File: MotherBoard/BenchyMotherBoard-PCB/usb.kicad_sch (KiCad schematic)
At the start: 1 part

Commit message: Add MORE regulators, USB, Display, and SDCard
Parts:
- added J? (x6): USB3_A, symbol Connector:USB3_A
- added U? (x3): USB7206C, SnapEDA:QFN40P1200X1200X90-101N, symbol Daxxn_IC:USB7206C
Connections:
- net MPU-USB-D+: now reaches U?.V14 (USB-DP1)
- net MPU-USB-D+: now also U?.42 (USBD-DP6)
- net MPU-USB-D-: now reaches U?.W14 (USB-DM1)
- net MPU-USB-D-: now also U?.41 (USBD-DM6)
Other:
- company: (none) -> Daxxn Industries
- title: (none) -> Benchy Version 2
- moved on the sheet: U?D

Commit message: Initial schematic lock
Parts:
- removed J?: USB3_A, symbol Connector:USB3_A
- removed U? (x2): USB7206C, SnapEDA:QFN40P1200X1200X90-101N, symbol Daxxn_IC:USB7206C
- added C139, C140, C142, C143, C144, C145, C146, C147, C148, C149, C156, C160, C? (x2): 10uF, Capacitor_SMD:C_1210_3225Metric, symbol Device:C_Small
- added C141, C150, C151, C152, C153, C154, C155, C163, C164: 100nF, Capacitor_SMD:C_0402_1005Metric, symbol Device:C_Small
- added C157, C161: 1uF, Capacitor_SMD:C_1210_3225Metric, symbol Device:C_Small
- added C158, C159, C162, C165: 15pF, Capacitor_SMD:C_0402_1005Metric, symbol Device:C_Small
- added C? (x3): 1uF, Capacitor_SMD:C_0805_2012Metric, symbol Device:C_Small
- added C?: 100nF, Capacitor_SMD:C_0805_2012Metric, symbol Device:C_Small
- added D1, D2, D3, D4, D5: ESDLC5V0PB8, Package_DFN_QFN:UDFN-9_1.0x3.8mm_P0.5mm, symbol Power_Protection:ESDLC5V0PB8
- added D6: PUSB3AB4, Daxxn_Packages:DFN2510A-10, symbol Daxxn_Protection:PUSB3AB4
- added D7: ORANGE, Daxxn_LEDs:LED-SMD-1204_RA, symbol Device:LED_Small
- added D8: YELLOW, Daxxn_LEDs:LED-SMD-1204_RA, symbol Device:LED_Small
- added J13, J14: USB_A, Daxxn_Connectors:1002-014-01000, symbol Connector:USB_A
- added J8: USB3_B, Daxxn_Connectors:USB-GSB3211311WEU, symbol Connector:USB3_B
- added J?: TFT-DISPLAY, symbol Connector:Conn_01x21_Male
- added JP1: WP-JMP, Connector_PinSocket_2.54mm:PinSocket_1x03_P2.54mm_Vertical, symbol Jumper:Jumper_3_Bridged12
- added Q?: RQ5A030AP, Package_TO_SOT_SMD:SOT-23, symbol Daxxn_Transistors:RQ5A030AP
- added R100: 3K, Resistor_SMD:R_0402_1005Metric, symbol Device:R_Small_US
- added R101, R107, R92, R93, R94, R95: 10K, Resistor_SMD:R_0402_1005Metric, symbol Device:R_Small_US
- added R102: 12K 1%, Resistor_SMD:R_0402_1005Metric, symbol Device:R_Small_US
- added R103, R104, R88: 50K, Resistor_SMD:R_0402_1005Metric, symbol Device:R_Small_US
- added R105, R106: 1K, Resistor_SMD:R_0402_1005Metric, symbol Device:R_Small_US
- added R108, R96, R97: 200K, Resistor_SMD:R_0402_1005Metric, symbol Device:R_Small_US
- added R87: 43K, Resistor_SMD:R_0402_1005Metric, symbol Device:R_Small_US
- added R89, R90, R91: 18K, Resistor_SMD:R_0402_1005Metric, symbol Device:R_Small_US
- added R98, R99, R? (x2): 2.2K, Resistor_SMD:R_0402_1005Metric, symbol Device:R_Small_US
- added R?: 10 1%, Resistor_SMD:R_0805_2012Metric, symbol Device:R_Small_US
- added R?: 330, Resistor_SMD:R_0805_2012Metric, symbol Device:R_Small_US
- added R?: 120, Resistor_SMD:R_0805_2012Metric, symbol Device:R_Small_US
- added R?: 10K, Daxxn_Switches:Bourns_TC33X, symbol Daxxn_Other:R_Pot_Small_US
- added U12, U13, U14: UCS2114, Daxxn_Packages:UCS2114T-1-V_LXVAO-Custom, symbol Daxxn_IC:UCS2114
- added U15: 24LC08, Package_SO:SOIC-8_3.9x4.9mm_P1.27mm, symbol Memory_EEPROM:24LC08
- added U16: USB2412, Package_DFN_QFN:QFN-28-1EP_5x5mm_P0.5mm_EP3.35x3.35mm, symbol Daxxn_IC:USB2412
- added unit 2 of U9
- added unit 3 of U9
- added U?: AS321, Package_TO_SOT_SMD:SOT-23-5, symbol Daxxn_OPAMP:AS321
- added U?: LM317L, Package_TO_SOT_SMD:SOT-89-3, symbol Regulator_Linear:LM317L_SOT-89
- added Y3, Y4: 25MHz, Daxxn_Passives:Crystal_SMD_4Pin_3.2x2.5mm, symbol Device:Crystal_GND24_Small
- J10, J11, J12, J7, J9: renamed from J?; footprint (none) -> Connector_USB:USB3_A_Molex_48393-001
- gave numbers to parts that had none: 2
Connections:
- net DSI-D0-: now reaches U2.A13 (DSI-D0N)
- net DSI-D0-: now also J?.18 (Pin_18)
- net DSI-CL-: now reaches U2.A14 (DSI-CKN)
- net DSI-CL-: now also J?.15 (Pin_15)
- net DSI-D1-: now reaches U2.A15 (DSI-D1N)
- net DSI-D1-: now also J?.12 (Pin_12)
- net DSI-D0+: now reaches U2.B13 (DSI-D0P)
- net DSI-D0+: now also J?.17 (Pin_17)
- net DSI-CL+: now reaches U2.B14 (DSI-CKP)
- net DSI-CL+: now also J?.14 (Pin_14)
- net DSI-D1+: now reaches U2.B15 (DSI-D1P)
- net DSI-D1+: now also J?.11 (Pin_11)
- net USB-INU-D-: now reaches U2.V13 (USB-DM2)
- net USB-INU-D-: now also U16.21 (USBU-)
- net at U2.V16 (USB-RREF): now also R100.1
- net USB-INU-D+: now reaches U2.W13 (USB-DP2)
- net USB-INU-D+: now also U16.22 (USBU+)
- net at J11.1 (VBUS): now also C147.2, U13.11 (VBUS2), U13.12 (VBUS2)
- net GND: now reaches J11.10 (SHIELD)
- net GND: now also J10.10 (SHIELD), J10.4 (GND), J10.7 (DRAIN), J11.4 (GND), J11.7 (DRAIN), J12.10 (SHIELD), J12.4 (GND), J12.7 (DRAIN), J7.10 (SHIELD), J7.4 (GND), J7.7 (DRAIN), J9.10 (SHIELD), J9.4 (GND), J9.7 (DRAIN), C139.1, C140.1, C141.1, C142.1, C143.1, C144.1, C145.1, C146.1, C147.1, C148.1, C149.1, C150.1, C151.1, C152.1, C153.1, C154.1, C155.1, C156.1, C157.1, C158.2, C159.1, C160.1, C161.1, C162.2, C163.1, C164.1, C165.1, C?.2, C?.2, C?.2, C?.2, C?.2, C?.2, D1.3 (A), D2.3 (A), D3.3 (A), D4.3 (A), D5.3 (A), D6.3 (A), D6.8 (A), J13.4 (GND), J13.5 (Shield), J14.4 (GND), J14.5 (Shield), J8.10 (SHIELD), J8.4 (GND), J8.7 (DRAIN), J?.10 (Pin_10), J?.13 (Pin_13), J?.16 (Pin_16), J?.19 (Pin_19), J?.2 (Pin_2), J?.20 (Pin_20), J?.21 (Pin_21), JP1.3 (B), R100.2, R102.2, R103.2, R104.2, R105.2, R106.2, R107.1, R108.1, R88.2, R89.2, R90.2, R91.2, R95.1, R96.1, R97.1, R?.3, U12.13 (BOOST), U12.14 (GND), U12.17 (GND), U12.2 (GND), U13.13 (BOOST), U13.14 (GND), U13.17 (GND), U13.2 (GND), U14.13 (BOOST), U14.14 (GND), U14.15 (EN2), U14.16 (ALERT2), U14.17 (GND), U14.2 (GND), U15.1 (A0), U15.2 (A1), U15.3 (A2), U15.4 (GND), U16.15 (TEST1), U16.29 (GND), U16.6 (TEST), U9.24 (TESTEN), U?.2 (V-), Y3.2, Y3.4, Y4.2, Y4.4
- net USB4-D-: now reaches J11.2 (D-)
- net USB4-D-: now also U9.35 (USBD-DM4), D4.2 (K2)
- net USB4-D+: now reaches J11.3 (D+)
- net USB4-D+: now also U9.34 (USBD-DP4), D4.4 (K3)
- net USB4-TX-: now reaches J11.5 (SSRX-)
- net USB4-TX-: now also U9.37 (USBD-TXM4), D4.5 (K4)
- net USB4-TX+: now reaches J11.6 (SSRX+)
- net USB4-TX+: now also U9.36 (USBD-TXP4), D4.6 (K5)
- net USB4-RX-: now reaches J11.8 (SSTX-)
- net USB4-RX-: now also U9.40 (USBD-RXM4), D4.7 (K6)
- net USB4-RX+: now reaches J11.9 (SSTX+)
- net USB4-RX+: now also U9.39 (USBD-RXP4), D4.8 (K7)
- net at J7.1 (VBUS): now also C140.2, U12.4 (VBUS1), U12.5 (VBUS1)
- net USB1-D-: now reaches J7.2 (D-)
- net USB1-D-: now also U9.6 (USBD-DM1), D1.2 (K2)
- net USB1-D+: now reaches J7.3 (D+)
- net USB1-D+: now also U9.5 (USBD-DP1), D1.4 (K3)
- net USB1-TX-: now reaches J7.5 (SSRX-)
- net USB1-TX-: now also U9.8 (USBD-TXM1), D1.5 (K4)
- net USB1-TX+: now reaches J7.6 (SSRX+)
- net USB1-TX+: now also U9.7 (USBD-TXP1), D1.6 (K5)
- net USB1-RX-: now reaches J7.8 (SSTX-)
- net USB1-RX-: now also U9.11 (USBD-RXM1), D1.7 (K6)
- net USB1-RX+: now reaches J7.9 (SSTX+)
- net USB1-RX+: now also U9.10 (USBD-RXP1), D1.8 (K7)
- net USB2-D+: now reaches U9.14 (USBD-DP2)
- net USB2-D+: now also J9.3 (D+), D2.4 (K3)
- net USB2-D-: now reaches U9.15 (USBD-DM2)
- net USB2-D-: now also J9.2 (D-), D2.2 (K2)
- net USB2-TX+: now reaches U9.16 (USBD-TXP2)
- net USB2-TX+: now also J9.6 (SSRX+), D2.6 (K5)
- net USB2-TX-: now reaches U9.17 (USBD-TXM2)
- net USB2-TX-: now also J9.5 (SSRX-), D2.5 (K4)
- net USB2-RX+: now reaches U9.19 (USBD-RXP2)
- net USB2-RX+: now also J9.9 (SSTX+), D2.8 (K7)
- net at U9.2 (VBUS-MON): now also R87.2, R88.1
- net USB2-RX-: now reaches U9.20 (USBD-RXM2)
- net USB2-RX-: now also J9.8 (SSTX-), D2.7 (K6)
- net USB3-D+: now reaches U9.27 (USBD-DP3)
- net USB3-D+: now also J10.3 (D+), D3.4 (K3)
- net USB3-D-: now reaches U9.28 (USBD-DM3)
- net USB3-D-: now also J10.2 (D-), D3.2 (K2)
- net USB3-TX+: now reaches U9.29 (USBD-TXP3)
- net USB3-TX+: now also J10.6 (SSRX+), D3.6 (K5)
- net USB3-TX-: now reaches U9.30 (USBD-TXM3)
- net USB3-TX-: now also J10.5 (SSRX-), D3.5 (K4)
- net USB3-RX+: now reaches U9.32 (USBD-RXP3)
- net USB3-RX+: now also J10.9 (SSTX+), D3.8 (K7)
- net USB3-RX-: now reaches U9.33 (USBD-RXM3)
- net USB3-RX-: now also J10.8 (SSTX-), D3.7 (K6)
- net USB5-D+: now reaches U9.81 (USBD-DP5)
- net USB5-D+: now also J12.3 (D+), D5.4 (K3)
- net USB5-D-: now reaches U9.82 (USBD-DM5)
- net USB5-D-: now also J12.2 (D-), D5.2 (K2)
- net USB5-TX+: now reaches U9.83 (USBD-TXP5)
- net USB5-TX+: now also J12.6 (SSRX+), D5.6 (K5)
- net USB5-TX-: now reaches U9.84 (USBD-TXM5)
- net USB5-TX-: now also J12.5 (SSRX-), D5.5 (K4)
- net USB5-RX+: now reaches U9.86 (USBD-RXP5)
- net USB5-RX+: now also J12.9 (SSTX+), D5.8 (K7)
- net USB5-RX-: now reaches U9.87 (USBD-RXM5)
- net USB5-RX-: now also J12.8 (SSTX-), D5.7 (K6)
- net USBU-D+: now reaches U9.89 (USBU-DP)
- net USBU-D+: now also J8.3 (D+)
- net USBU-D-: now reaches U9.90 (USBU-DM)
- net USBU-D-: now also J8.2 (D-)
- net USBU-TX+: now reaches U9.91 (USBU-TXP)
- net USBU-TX+: now also J8.6 (SSTX+)
- net USBU-TX-: now reaches U9.92 (USBU-TXM)
- net USBU-TX-: now also J8.5 (SSTX-)
- net USBU-RX+: now reaches U9.94 (USBU-RXP)
- net USBU-RX+: now also J8.9 (SSRX+)
- net USBU-RX-: now reaches U9.95 (USBU-RXM)
- net USBU-RX-: now also J8.8 (SSRX-)
- net at J9.1 (VBUS): now also C143.2, U12.11 (VBUS2), U12.12 (VBUS2)
- net at J12.1 (VBUS): now also C149.2, U14.4 (VBUS1), U14.5 (VBUS1)
- net at J10.1 (VBUS): now also C145.2, U13.4 (VBUS1), U13.5 (VBUS1)
- net MPU-USB-D+ renamed USB-MPU-D+
- net MPU-USB-D- renamed USB-MPU-D-
- new net: R104.1, U16.13 (NON-REM1)
- new net: C162.1, U9.97 (XTAL0), Y4.1
- new net: Q?.1 (G), R?.2
- new net: Q?.3 (D), R?.2, U?.3 (IN-)
- new net: R98.1, U15.6 (SCL), U9.3 (PF31)
- new net: R96.2, U9.22 (CFG-STRAP2)
- new net: R92.1, U9.63 (TEST1)
- new net: D7.2 (A), R103.1, U16.19 (SUSP-IND/NON-REM0)
- new net: C?.1, C?.1, R?.1, R?.1, U?.2 (VO)
- new net: D7.1 (K), R105.1
- new net: C141.2, J8.1 (VBUS), R87.1
- new net: C?.1, R?.2, U?.1 (IN+)
- new net: R?.1, U?.4 (OUT)
- new net: R97.2, U9.23 (CFG-STRAP3)
- new net: JP1.2 (C), U15.7 (WP)
- new net: R?.2, U?.1 (ADJ)
- new net: R95.2, U9.21 (CFG-STRAP1)
- new net: R99.1, U15.5 (SDA), U9.61 (PF18)
- new net: R93.1, U9.64 (TEST2)
- new net: R94.1, U9.65 (TEST3)
- new net: C163.2, U16.9 (CRFILT)
- new net: D8.2 (A), U16.16 (HS-IND)
- new net: C158.1, U16.23 (XTALOUT), Y3.1
- new net: C159.2, U16.24 (XTALIN), Y3.3
- new net: C164.2, U16.25 (PLLFILT)
- new net: R102.1, U16.26 (RBIAS)
- new net: C165.2, U9.98 (XTAL1), Y4.3
- new net: R91.1, U14.3 (COMM-EN)
- new net: D8.1 (K), R106.1
- new net: D6.10 (NC), D6.6 (NC), D6.7 (NC), D6.9 (NC)
- new net: R89.1, U12.3 (COMM-EN)
- new net: R108.2, U9.70 (SPI-D0)
- new net: R90.1, U13.3 (COMM-EN)
- new net: R107.2, U9.69 (~{SPI_CE})
- new net +30V: C?.1, C?.1, C?.1, U?.3 (VI), U?.5 (V+)
- new net BK-ANODE: J?.4 (Pin_4), Q?.2 (S)
- new net DISP-USB-BUS.BRIGHT: R?.1
- new net DISP-USB-BUS.TE: J?.8 (Pin_8)
- new net DISP-USB-BUS.USB-RESET: R101.1, U16.17 (~{RESET}), U9.1 (~{RESET})
- new net DISP-USB-BUS.USB-SCK: R?.2, U12.19 (I2C-SCLK), U13.19 (I2C-SCLK), U14.19 (I2C-SCLK)
- new net DISP-USB-BUS.USB-SDA: R?.2, U12.18 (I2C-SDA), U13.18 (I2C-SDA), U14.18 (I2C-SDA)
- new net RESET: J?.9 (Pin_9)
- new net USB-IN1-D+: D6.1 (K1), J13.3 (D+), U16.1 (USBD1-D+)
- new net USB-IN1-D-: D6.2 (K2), J13.2 (D-), U16.28 (USBD1-)
- new net USB-IN2-D+: D6.4 (K3), J14.3 (D+), U16.3 (USBD2-D+)
- new net USB-IN2-D-: D6.5 (K4), J14.2 (D-), U16.2 (USBD2-D-)
- new net USB1-EN-~{OC}: U12.1 (EN1), U12.20 (ALERT1), U9.60 (PF17)
- new net USB2-EN-~{OC}: U12.15 (EN2), U12.16 (ALERT2), U9.59 (PF16)
- new net USB3-EN-~{OC}: U13.1 (EN1), U13.20 (ALERT1), U9.58 (PF15)
- new net USB4-EN-~{OC}: U13.15 (EN2), U13.16 (ALERT2), U9.57 (PF14)
- new net USB5-EN-~{OC}: U14.1 (EN1), U14.20 (ALERT1), U9.56 (PF13)
- new net VCC: C139.2, C142.2, C144.2, C146.2, C148.2, C156.2, C157.2, C160.2, C161.2, J13.1 (VBUS), J14.1 (VBUS), U12.10 (VS), U12.6 (VS), U12.7 (VS), U12.8 (VDD), U12.9 (VS), U13.10 (VS), U13.6 (VS), U13.7 (VS), U13.8 (VDD), U13.9 (VS), U14.6 (VS), U14.7 (VS), U14.8 (VDD)
- new net VDD: C150.2, C151.2, C152.2, C153.2, C154.2, C155.2, J?.6 (Pin_6), J?.7 (Pin_7), JP1.1 (A), R101.2, R92.2, R93.2, R94.2, R98.2, R99.2, R?.1, R?.1, U15.8 (VCC), U16.10 (VDD), U16.14 (VDD), U16.20 (VDD), U16.27 (VDD), U16.4 (VDD)
- no-connect marks 0 -> 38
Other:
- moved on the sheet: J10, J11, J12, J7, J9, U2D

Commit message: (WIP) Start layout
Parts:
- J11: renamed from J9; footprint Connector_USB:USB3_A_Molex_48393-001 -> Daxxn_Connectors:GSB4116341HR
- J12: renamed from J10; footprint Connector_USB:USB3_A_Molex_48393-001 -> Daxxn_Connectors:GSB4116341HR
- J13: renamed from J11; footprint Connector_USB:USB3_A_Molex_48393-001 -> Daxxn_Connectors:GSB4116341HR
- J14: renamed from J12; footprint Connector_USB:USB3_A_Molex_48393-001 -> Daxxn_Connectors:GSB4116341HR
- J16: renamed from J?; footprint (none) -> Daxxn_Connectors:FH12A-20S-0.5SH55
- J9: renamed from J7; footprint Connector_USB:USB3_A_Molex_48393-001 -> Daxxn_Connectors:GSB4116341HR
- U10: renamed from U9; footprint SnapEDA:QFN40P1200X1200X90-101N -> Daxxn_Packages:100-VQFN-GND_12X12
- gave numbers to parts that had none: 15
- renumbered C139 to C141, C140 to C142, C141 to C143, C142 to C144, C143 to C145, C144 to C146, C145 to C147, C146 to C148, C147 to C149, C148 to C150, C149 to C151, C150 to C158, C151 to C159, C152 to C160, C153 to C161, C154 to C162, C155 to C163, C156 to C164, C157 to C165, C158 to C166, C159 to C167, C160 to C168, C161 to C169, C162 to C170, C163 to C171, C164 to C172, C165 to C173, J8 to J10, J13 to J15, J14 to J17, JP1 to JP2, R91 to R100, R92 to R101, R93 to R102, R94 to R103, R95 to R108, R96 to R109, R97 to R110, R98 to R111, R99 to R112, R100 to R113, R101 to R114, R102 to R115, R103 to R116, R104 to R117, R105 to R118, R106 to R119, R107 to R120, R108 to R121, R87 to R94, R88 to R95, R89 to R98, R90 to R99, U9 to U10, U12 to U13, U13 to U14, U14 to U15, U15 to U18, U16 to U19
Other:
- title: Benchy Version 2 -> Benchy Reloaded

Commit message: (WIP) Replaced DDR VRef with reg and started layout
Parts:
- added D9: ESDLC5V0PB8, Package_DFN_QFN:UDFN-9_1.0x3.8mm_P0.5mm, symbol Power_Protection:ESDLC5V0PB8
- J11: value USB3_A -> USB3-PORT2
- J12: value USB3_A -> USB3-PORT3
- J13: value USB3_A -> USB3-PORT4
- J14: value USB3_A -> USB3-PORT5
- J15: value USB_A -> USB-INTERNAL-PORT1
- J17: value USB_A -> USB-INTERNAL-PORT2
- J9: value USB3_A -> USB3-PORT1
- U10: footprint SnapEDA:QFN40P1200X1200X90-101N -> Daxxn_Packages:100-VQFN-GND_12X12
- renumbered C141 to C145, C142 to C146, C143 to C147, C144 to C148, C145 to C149, C146 to C150, C147 to C151, C148 to C152, C149 to C153, C150 to C154, C151 to C155, C152 to C156, C153 to C157, C154 to C158, C155 to C159, C156 to C160, C157 to C161, C158 to C162, C159 to C163, C160 to C164, C161 to C165, C162 to C166, C163 to C167, C164 to C168, C165 to C169, C166 to C170, C167 to C171, C168 to C172, C169 to C173, C170 to C174, C171 to C175, C172 to C176, C173 to C177, R103 to R100, R104 to R101, R105 to R102, R106 to R103, R107 to R104, R108 to R105, R109 to R106, R110 to R107, R111 to R108, R112 to R109, R113 to R110, R114 to R111, R115 to R112, R116 to R113, R117 to R114, R118 to R115, R119 to R116, R120 to R117, R121 to R118, R94 to R91, R95 to R92, R96 to R93, R97 to R94, R98 to R95, R99 to R96, R100 to R97, R101 to R98, R102 to R99, U2 to U1, U13 to U12, U14 to U13, U15 to U14, U16 to U15, U17 to U16, U18 to U17, U19 to U18
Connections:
- net DSI-CL+: now also D9.8 (K7)
- net DSI-CL-: now also D9.7 (K6)
- net DSI-D0+: now also D9.4 (K3)
- net DSI-D0-: now also D9.6 (K5)
- net DSI-D1+: now also D9.9 (K8)
- net DSI-D1-: now also D9.2 (K2)
- net GND: now also D9.3 (A)
- net USB-NONREM1: now reaches R114.1, U18.13 (NON-REM1)
- net USBP2-VBUS: now reaches C149.2, J11.1 (VBUS), U12.11 (VBUS2), U12.12 (VBUS2)
- net USB-SUSP-IND: now reaches D7.2 (A), R113.1, U18.19 (SUSP-IND/NON-REM0)
- net USB-RREF: now reaches R110.1, U1.V16 (USB-RREF)
- net USBP1-VBUS: now reaches C146.2, J9.1 (VBUS), U12.4 (VBUS1), U12.5 (VBUS1)
- net USBP4-VBUS: now reaches C153.2, J13.1 (VBUS), U13.11 (VBUS2), U13.12 (VBUS2)
- net USB-HS-IND: now reaches D8.2 (A), U18.16 (HS-IND)
- net USB-IN-XIN: now reaches C170.1, Y3.1
- net USB-IN-XIN: now also U18.24 (XTALIN); no longer U18.23 (XTALOUT)
- net USB-IN-XOUT: now reaches C171.2, Y3.3
- net USB-IN-XOUT: now also U18.23 (XTALOUT); no longer U18.24 (XTALIN)
- net USBP3-VBUS: now reaches C151.2, J12.1 (VBUS), U13.4 (VBUS1), U13.5 (VBUS1)
- net USB13-COMM: now reaches R97.1, U14.3 (COMM-EN)
- net USB13-COMM: now also R96.1, U13.3 (COMM-EN)
- net USB12-COMM: now reaches R95.1, U12.3 (COMM-EN)
- net USBP5-VBUS: now reaches C155.2, J14.1 (VBUS), U14.4 (VBUS1), U14.5 (VBUS1)
- net DISP-USB-BUS.BRIGHT renamed USB-BUS.BRIGHT
- net DISP-USB-BUS.TE renamed DISP-BUS.TE
- net DISP-USB-BUS.USB-RESET renamed USB-BUS.RESET
- net DISP-USB-BUS.USB-SCK renamed USB-BUS.SCK
- net DISP-USB-BUS.USB-SDA renamed USB-BUS.SDA
- net RESET renamed DISP-BUS.RESET
- no-connect marks 38 -> 40
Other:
- moved on the sheet: C145, C146, C147, C148, C149, C150, C151, C152, C153, C154, C155, C156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

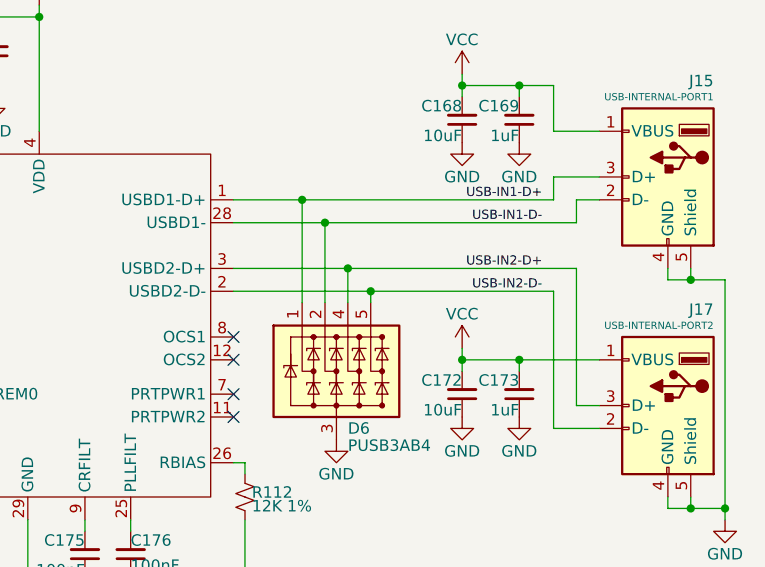
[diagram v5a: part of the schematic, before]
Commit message: Finish DDR3 memory layout
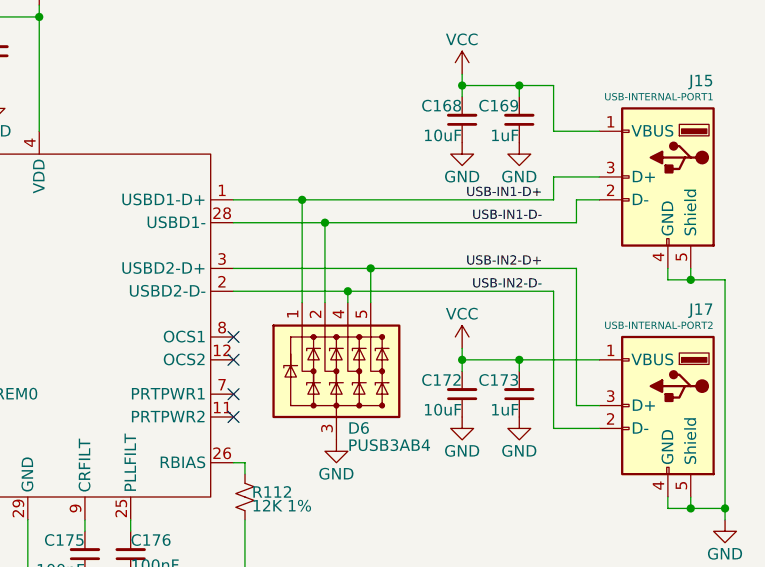
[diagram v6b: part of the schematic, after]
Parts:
- D1, D2, D3, D4, D5, D9: footprint Package_DFN_QFN:UDFN-9_1.0x3.8mm_P0.5mm -> Daxxn_Packages:U-DFN3810-9
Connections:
- net USB-IN2-D+: now also D6.5 (K4); no longer D6.4 (K3)
- net USB-IN2-D-: now also D6.4 (K3); no longer D6.5 (K4)
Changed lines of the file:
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@@
   (junction (at 204.47 24.13) (diameter 0) (color 0 0 0 0)
   )
-  (junction (at 365.76 212.09) (diameter 0) (color 0 0 0 0)
-  )
   (junction (at 168.91 226.06) (diameter 0) (color 0 0 0 0)
   )
@@
   (junction (at 401.32 78.74) (diameter 0) (color 0 0 0 0)
   )
+  (junction (at 363.22 212.09) (diameter 0) (color 0 0 0 0)
+  )
   (junction (at 322.58 245.11) (diameter 0) (color 0 0 0 0)
   )
@@
   (junction (at 375.92 69.85) (diameter 0) (color 0 0 0 0)
   )
-  (junction (at 363.22 209.55) (diameter 0) (color 0 0 0 0)
-  )
   (junction (at 246.38 111.76) (diameter 0) (color 0 0 0 0)
   )
@@
   (junction (at 303.53 140.97) (diameter 0) (color 0 0 0 0)
   )
+  (junction (at 365.76 209.55) (diameter 0) (color 0 0 0 0)
+  )
   (junction (at 185.42 104.14) (diameter 0) (color 0 0 0 0)
   )
@@
     (stroke (width 0) (type default))
   )
-  (wire (pts (xy 363.22 209.55) (xy 363.22 213.36))
-    (stroke (width 0) (type default))
-  )
   (wire (pts (xy 251.46 86.36) (xy 280.67 86.36))
     (stroke (width 0) (type default))
@@
     (stroke (width 0) (type default))
   )
+  (wire (pts (xy 363.22 212.09) (xy 386.08 212.09))
+    (stroke (width 0) (type default))
+  )
   (wire (pts (xy 107.95 58.42) (xy 121.92 58.42))
     (stroke (width 0) (type default))
@@
     (stroke (width 0) (type default))
   )
+  (wire (pts (xy 365.76 209.55) (xy 365.76 213.36))
+    (stroke (width 0) (type default))
+  )
   (wire (pts (xy 270.51 203.2) (xy 278.13 203.2))
     (stroke (width 0) (type default))
@@
     (stroke (width 0) (type default))
   )
-  (wire (pts (xy 350.52 209.55) (xy 363.22 209.55))
+  (wire (pts (xy 350.52 209.55) (xy 365.76 209.55))
     (stroke (width 0) (type default))
   )
@@
     (stroke (width 0) (type default))
   )
-  (wire (pts (xy 365.76 212.09) (xy 386.08 212.09))
+  (wire (pts (xy 350.52 212.09) (xy 363.22 212.09))
     (stroke (width 0) (type default))
   )
@@
     (stroke (width 0) (type default))
   )
+  (wire (pts (xy 365.76 209.55) (xy 388.62 209.55))
+    (stroke (width 0) (type default))
+  )
   (wire (pts (xy 346.71 72.39) (xy 378.46 72.39))
     (stroke (width 0) (type default))
@@
     (stroke (width 0) (type default))
   )
-  (wire (pts (xy 365.76 212.09) (xy 365.76 213.36))
-    (stroke (width 0) (type default))
-  )
   (wire (pts (xy 107.95 172.72) (xy 113.03 172.72))
     (stroke (width 0) (type default))
@@
     (stroke (width 0) (type default))
   )
-  (wire (pts (xy 350.52 212.09) (xy 365.76 212.09))
-    (stroke (width 0) (type default))
-  )
   (wire (pts (xy 182.88 67.31) (xy 198.12 67.31))
     (stroke (width 0) (type default))
@@
     (stroke (width 0) (type default))
   )
-  (wire (pts (xy 363.22 209.55) (xy 388.62 209.55))
-    (stroke (width 0) (type default))
-  )
   (wire (pts (xy 157.48 95.25) (xy 154.94 95.25))
     (stroke (width 0) (type default))
@@
     (stroke (width 0) (type default))
   )
+  (wire (pts (xy 363.22 212.09) (xy 363.22 213.36))
+    (stroke (width 0) (type default))
+  )
   (wire (pts (xy 370.84 62.23) (xy 383.54 62.23))
     (stroke (width 0) (type default))
@@
       (effects (font (size 1.27 1.27)) (justify left))
     )
-    (property "Footprint" "Package_DFN_QFN:UDFN-9_1.0x3.8mm_P0.5mm" (at 384.81 128.27 0)
+    (property "Footprint" "Daxxn_Packages:U-DFN3810-9" (at 384.81 128.27 0)
       (effects (font (size 1.27 1.27)) (justify left) hide)
     )
@@
       (effects (font (size 1.27 1.27)) hide)
     )
+    (property "Schematic" "" (at 370.84 127 0)
+      (effects (font (size 1.27 1.27)) hide)
+    )
+    (property "PartNumber" "" (at 370.84 127 0)
+      (effects (font (size 1.27 1.27)))
+    )
+    (property "SupplierPN" "" (at 370.84 127 0)
+      (effects (font (size 1.27 1.27)) hide)
+    )
     (pin "3")
     (pin "1")
@@
       (effects (font (size 1.27 1.27)) (justify left))
     )
-    (property "Footprint" "Package_DFN_QFN:UDFN-9_1.0x3.8mm_P0.5mm" (at 289.56 99.06 0)
+    (property "Footprint" "Daxxn_Packages:U-DFN3810-9" (at 289.56 99.06 0)
       (effects (font (size 1.27 1.27)) (justify left) hide)
     )
@@
       (effects (font (size 1.27 1.27)) hide)
     )
+    (property "Schematic" "" (at 275.59 97.79 0)
+      (effects (font (size 1.27 1.27)) hide)
+    )
+    (property "PartNumber" "" (at 275.59 97.79 0)
+      (effects (font (size 1.27 1.27)))
+    )
+    (property "SupplierPN" "" (at 275.59 97.79 0)
+      (effects (font (size 1.27 1.27)) hide)
+    )
     (pin "3")
     (pin "1")
@@
       (effects (font (size 1.27 1.27)) (justify left))
     )
-    (property "Footprint" "Package_DFN_QFN:UDFN-9_1.0x3.8mm_P0.5mm" (at 289.56 144.78 0)
+    (property "Footprint" "Daxxn_Packages:U-DFN3810-9" (at 289.56 144.78 0)
       (effects (font (size 1.27 1.27)) (justify left) hide)
     )
@@
       (effects (font (size 1.27 1.27)) hide)
     )
+    (property "Schematic" "" (at 275.59 143.51 0)
+      (effects (font (size 1.27 1.27)) hide)
+    )
+    (property "PartNumber" "" (at 275.59 143.51 0)
+      (effects (font (size 1.27 1.27)))
+    )
+    (property "SupplierPN" "" (at 275.59 143.51 0)
+      (effects (font (size 1.27 1.27)) hide)
+    )
     (pin "3")
     (pin "1")
@@
       (effects (font (size 1.27 1.27)) (justify left))
     )
-    (property "Footprint" "Package_DFN_QFN:UDFN-9_1.0x3.8mm_P0.5mm" (at 177.8 245.11 0)
+    (property "Footprint" "Daxxn_Packages:U-DFN3810-9" (at 177.8 245.11 0)
       (effects (font (size 1.27 1.27)) (justify left) hide)
     )
@@
       (effects (font (size 1.27 1.27)) hide)
     )
+    (property "Schematic" "" (at 163.83 243.84 0)
+      (effects (font (size 1.27 1.27)) hide)
+    )
+    (property "PartNumber" "" (at 163.83 243.84 0)
+      (effects (font (size 1.27 1.27)))
+    )
+    (property "SupplierPN" "" (at 163.83 243.84 0)
+      (effects (font (size 1.27 1.27)) hide)
+    )
     (pin "3")
     (pin "1")
@@
       (effects (font (size 1.27 1.27)) hide)
     )
+    (property "Schematic" "" (at 309.88 196.85 0)
+      (effects (font (size 1.27 1.27)) hide)
+    )
+    (property "PartNumber" "" (at 309.88 196.85 0)
+      (effects (font (size 1.27 1.27)))
+    )
+    (property "SupplierPN" "" (at 309.88 196.85 0)
+      (effects (font (size 1.27 1.27)) hide)
+    )
     (pin "1")
     (pin "10")
@@
       (effects (font (size 1.27 1.27)) (justify left))
     )
-    (property "Footprint" "Package_DFN_QFN:UDFN-9_1.0x3.8mm_P0.5mm" (at 384.81 82.55 0)
+    (property "Footprint" "Daxxn_Packages:U-DFN3810-9" (at 384.81 82.55 0)
       (effects (font (size 1.27 1.27)) (justify left) hide)
     )
@@
       (effects (font (size 1.27 1.27)) hide)
     )
+    (property "Schematic" "" (at 370.84 81.28 0)
+      (effects (font (size 1.27 1.27)) hide)
+    )
+    (property "PartNumber" "" (at 370.84 81.28 0)
+      (effects (font (size 1.27 1.27)))
+    )
+    (property "SupplierPN" "" (at 370.84 81.28 0)
+      (effects (font (size 1.27 1.27)) hide)
+    )
     (pin "3")
     (pin "1")
@@
       (effects (font (size 1.27 1.27)) (justify left))
     )
-    (property "Footprint" "Package_DFN_QFN:UDFN-9_1.0x3.8mm_P0.5mm" (at 289.56 53.34 0)
+    (property "Footprint" "Daxxn_Packages:U-DFN3810-9" (at 289.56 53.34 0)
       (effects (font (size 1.27 1.27)) (justify left) hide)
     )
@@
       (effects (font (size 1.27 1.27)) hide)
     )
+    (property "Schematic" "" (at 275.59 52.07 0)
+      (effects (font (size 1.27 1.27)) hide)
+    )
+    (property "PartNumber" "" (at 275.59 52.07 0)
+      (effects (font (size 1.27 1.27)))
+    )
+    (property "SupplierPN" "" (at 275.59 52.07 0)
+      (effects (font (size 1.27 1.27)) hide)
+    )
